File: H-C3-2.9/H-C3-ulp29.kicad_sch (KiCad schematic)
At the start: 55 parts, among them CN1 HX JN1.27-2X5 TP H4.9, J1 USB_C_Receptacle_USB2.0, J2 AFC24-S24FIC-00, J4 SM04B-SRSS-TB_LF__SN_, Q1 Si1308, Q2 Si2301CDS, SW1 K2-1806SQ-A2DW-04, SW2 K2-1806SQ-A2DW-04, SW3 K2-1806SQ-A2DW-04, U1 E73-2G4M08S1C, U2 MCP1700-3302E_SOT23, U8 PCF8563T, Y1 Crystal_Small, Y2 RTC_Crystal_32MHz

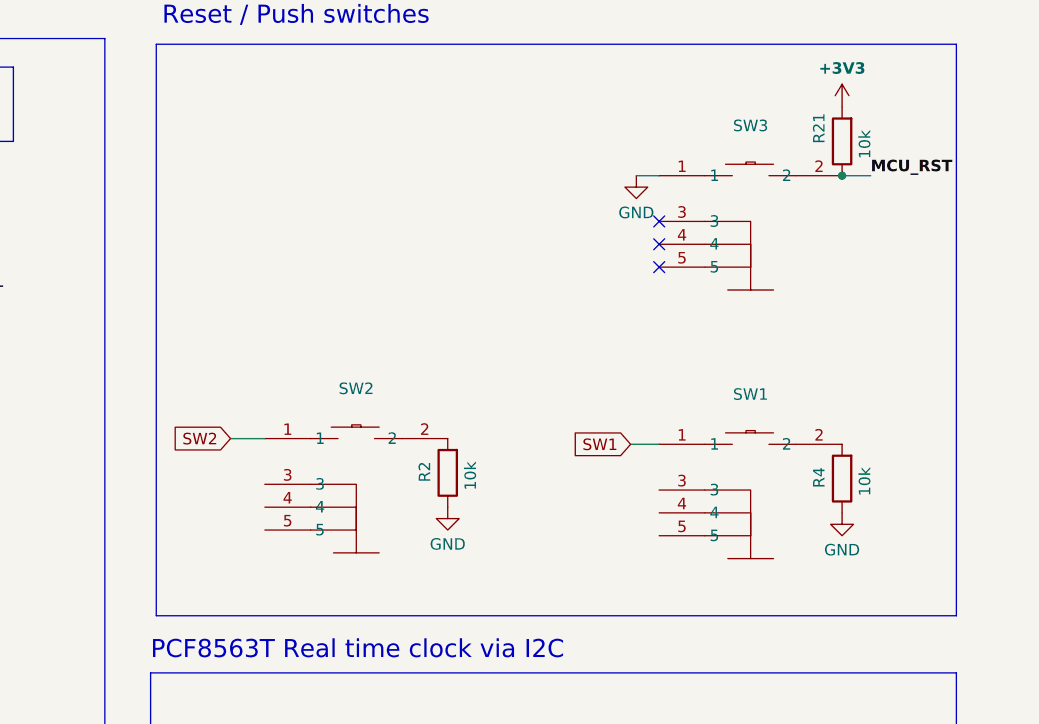
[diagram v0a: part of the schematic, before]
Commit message: Placing new knob
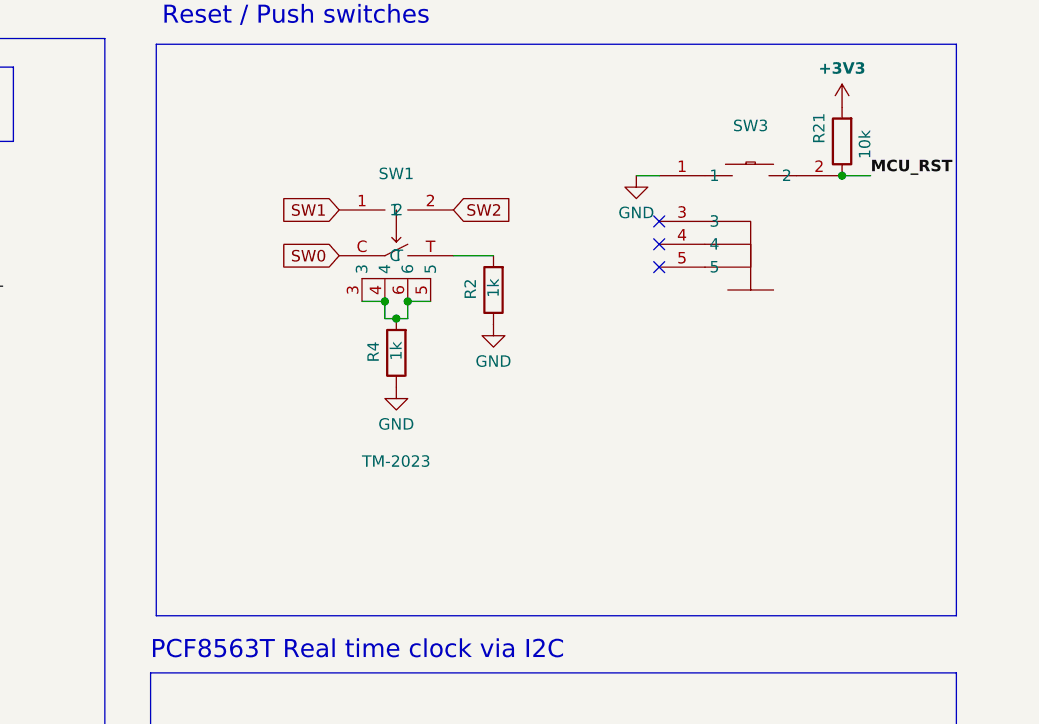
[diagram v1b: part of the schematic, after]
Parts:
- removed SW1, SW2: K2-1806SQ-A2DW-04, footprints:KEY-SMD_K2-1806SQ-A3DW-04, symbol easyeda:K2-1806SQ-A2DW-04
- added SW1: TM-2023, footprints:C318951_TM-2023-1, symbol easyeda:TM-2023
- R2, R4: value 10k -> 1k; LCSC C4322213 -> C11702
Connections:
- net SW1: now also SW1.1
- net SW2: now also SW1.2
- net at R2.2: now also SW1.T
- net at R4.2: now also SW1.3, SW1.4, SW1.5, SW1.6
- new net SW0: SW1.C
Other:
- moved on the sheet: R2, R4
